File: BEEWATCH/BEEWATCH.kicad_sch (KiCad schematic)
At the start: 0 parts

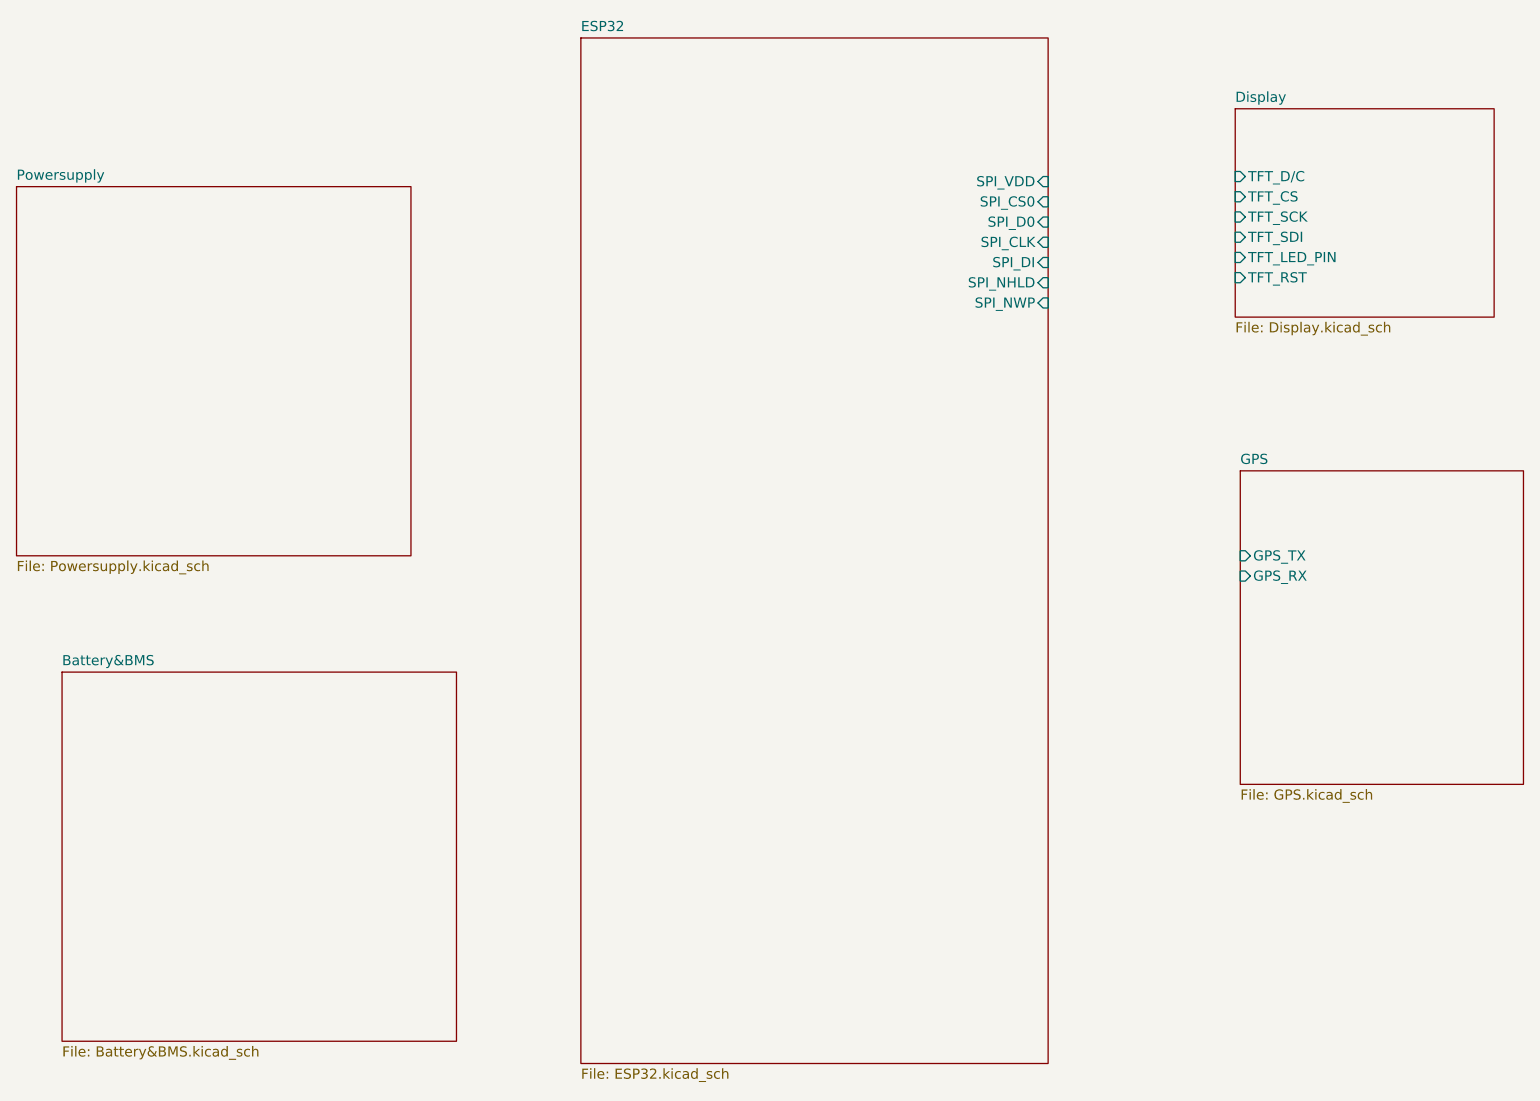
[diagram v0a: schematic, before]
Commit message: Inverted F Antenna designed
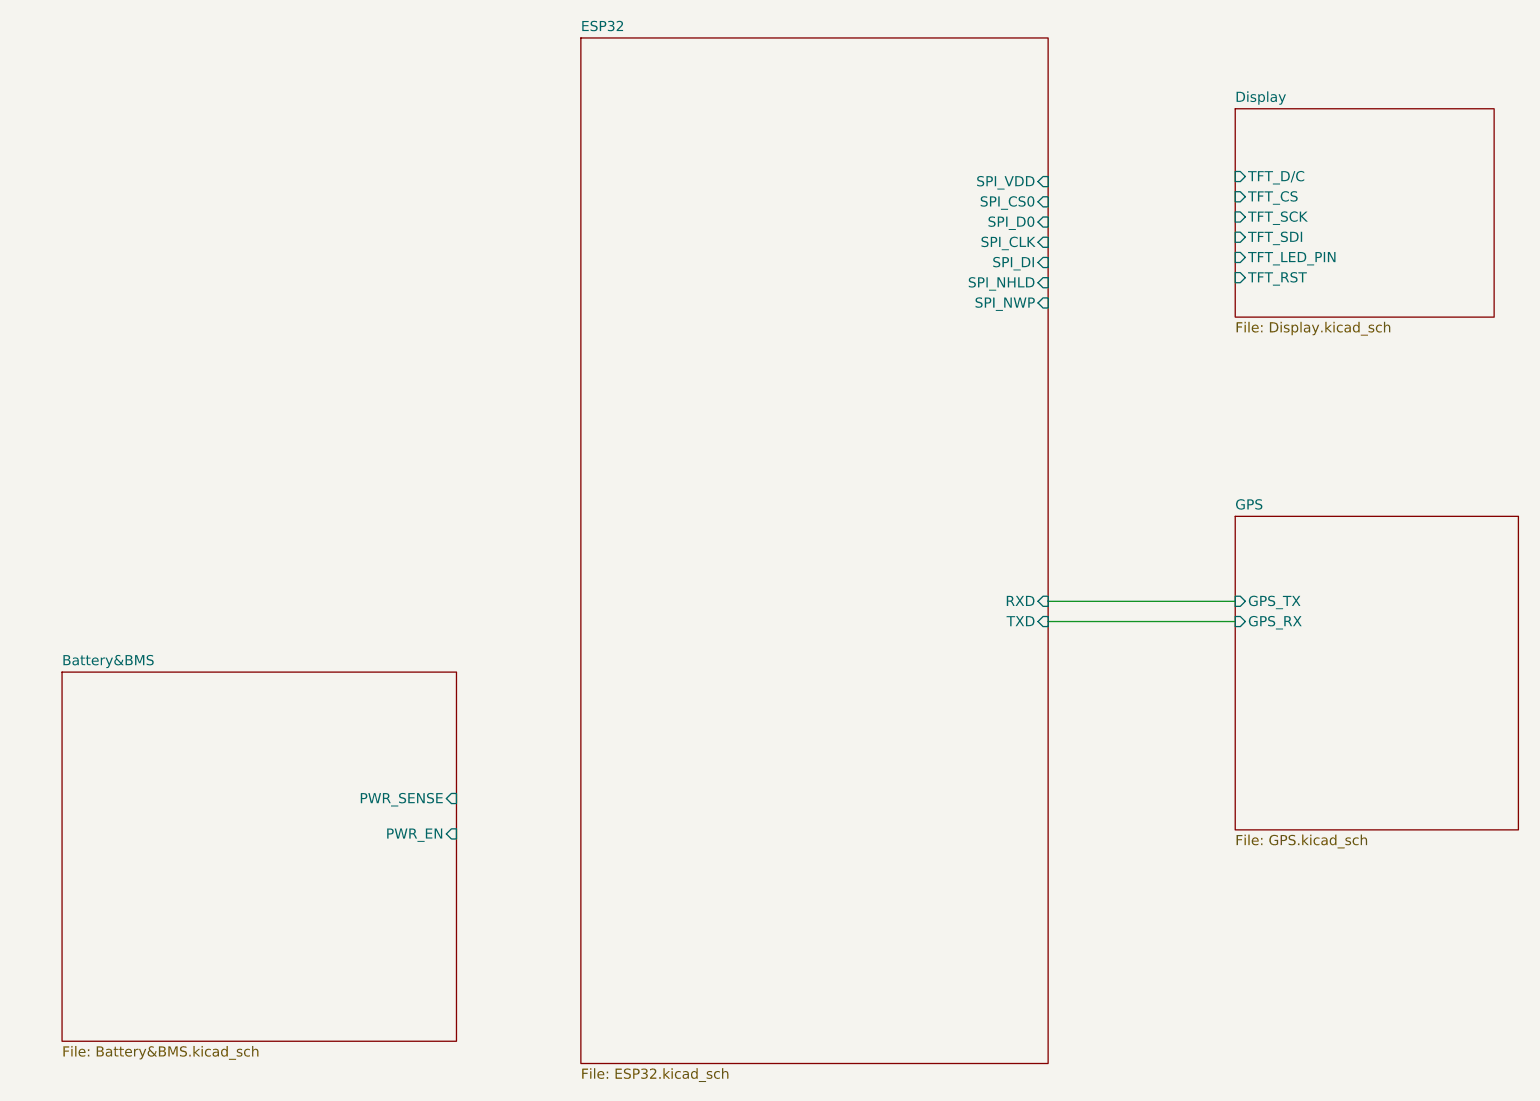
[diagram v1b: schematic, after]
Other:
- removed sheet Powersupply
- sheet Battery&BMS ports: added PWR_EN, PWR_SENSE; removed none
- sheet ESP32 ports: added RXD, TXD; removed none
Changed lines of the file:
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@@
 (kicad_sch (version 20230121) (generator eeschema)
   (paper "A4")
+  (wire (pts (xy 183.515 100.965) (xy 207.01 100.965))
+    (stroke (width 0) (type default))
+  )
+  (wire (pts (xy 183.515 98.425) (xy 207.01 98.425))
+    (stroke (width 0) (type default))
+  )
   (sheet (at 207.01 36.576) (size 32.512 26.162) (fields_autoplaced)
     (stroke (width 0.1524) (type solid))
@@
     )
   )
-  (sheet (at 207.645 82.042) (size 35.56 39.37) (fields_autoplaced)
+  (sheet (at 207.01 87.757) (size 35.56 39.37) (fields_autoplaced)
     (stroke (width 0.1524) (type solid))
     (fill (color 0 0 0 0.0000))
-    (property "Sheetname" "GPS" (at 207.645 81.3304 0)
+    (property "Sheetname" "GPS" (at 207.01 87.0454 0)
       (effects (font (size 1.27 1.27)) (justify left bottom))
     )
-    (property "Sheetfile" "GPS.kicad_sch" (at 207.645 121.9966 0)
+    (property "Sheetfile" "GPS.kicad_sch" (at 207.01 127.7116 0)
       (effects (font (size 1.27 1.27)) (justify left top))
     )
-    (pin "GPS_TX" input (at 207.645 92.71 180)
+    (pin "GPS_TX" input (at 207.01 98.425 180)
       (effects (font (size 1.27 1.27)) (justify left))
     )
-    (pin "GPS_RX" input (at 207.645 95.25 180)
+    (pin "GPS_RX" input (at 207.01 100.965 180)
       (effects (font (size 1.27 1.27)) (justify left))
     )
@@
       (effects (font (size 1.27 1.27)) (justify right))
     )
+    (pin "TXD" input (at 183.515 100.965 0)
+      (effects (font (size 1.27 1.27)) (justify right))
+    )
+    (pin "RXD" input (at 183.515 98.425 0)
+      (effects (font (size 1.27 1.27)) (justify right))
+    )
     (instances
       (project "BEEWATCH"
@@
       (effects (font (size 1.27 1.27)) (justify left top))
     )
+    (pin "PWR_SENSE" input (at 109.22 123.19 0)
+      (effects (font (size 1.27 1.27)) (justify right))
+    )
+    (pin "PWR_EN" input (at 109.22 127.635 0)
+      (effects (font (size 1.27 1.27)) (justify right))
+    )
     (instances
       (project "BEEWATCH"
@@
       )
     )
-  )
-  (sheet (at 53.975 46.355) (size 49.53 46.355) (fields_autoplaced)
-    (stroke (width 0.1524) (type solid))
-    (fill (color 0 0 0 0.0000))
-    (property "Sheetname" "Powersupply" (at 53.975 45.6434 0)
-      (effects (font (size 1.27 1.27)) (justify left bottom))
-    )
-    (property "Sheetfile" "Powersupply.kicad_sch" (at 53.975 93.2946 0)
-      (effects (font (size 1.27 1.27)) (justify left top))
-    )
-    (instances
-      (project "BEEWATCH"
-        (path "/e9c5fb53-480b-4989-8495-a3341ee99514" (page "5"))
-      )
-    )
